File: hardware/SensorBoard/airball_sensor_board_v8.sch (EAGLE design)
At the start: 61 parts, among them IC1 CP2102, J2 USB Female Type C Connector, T1 BC846, T2 BC846, U1 BQ24075, U2 BQ27441-G1, U3 BMP388, U4 ESP-WROOM-32, U7 SP0503BAHT

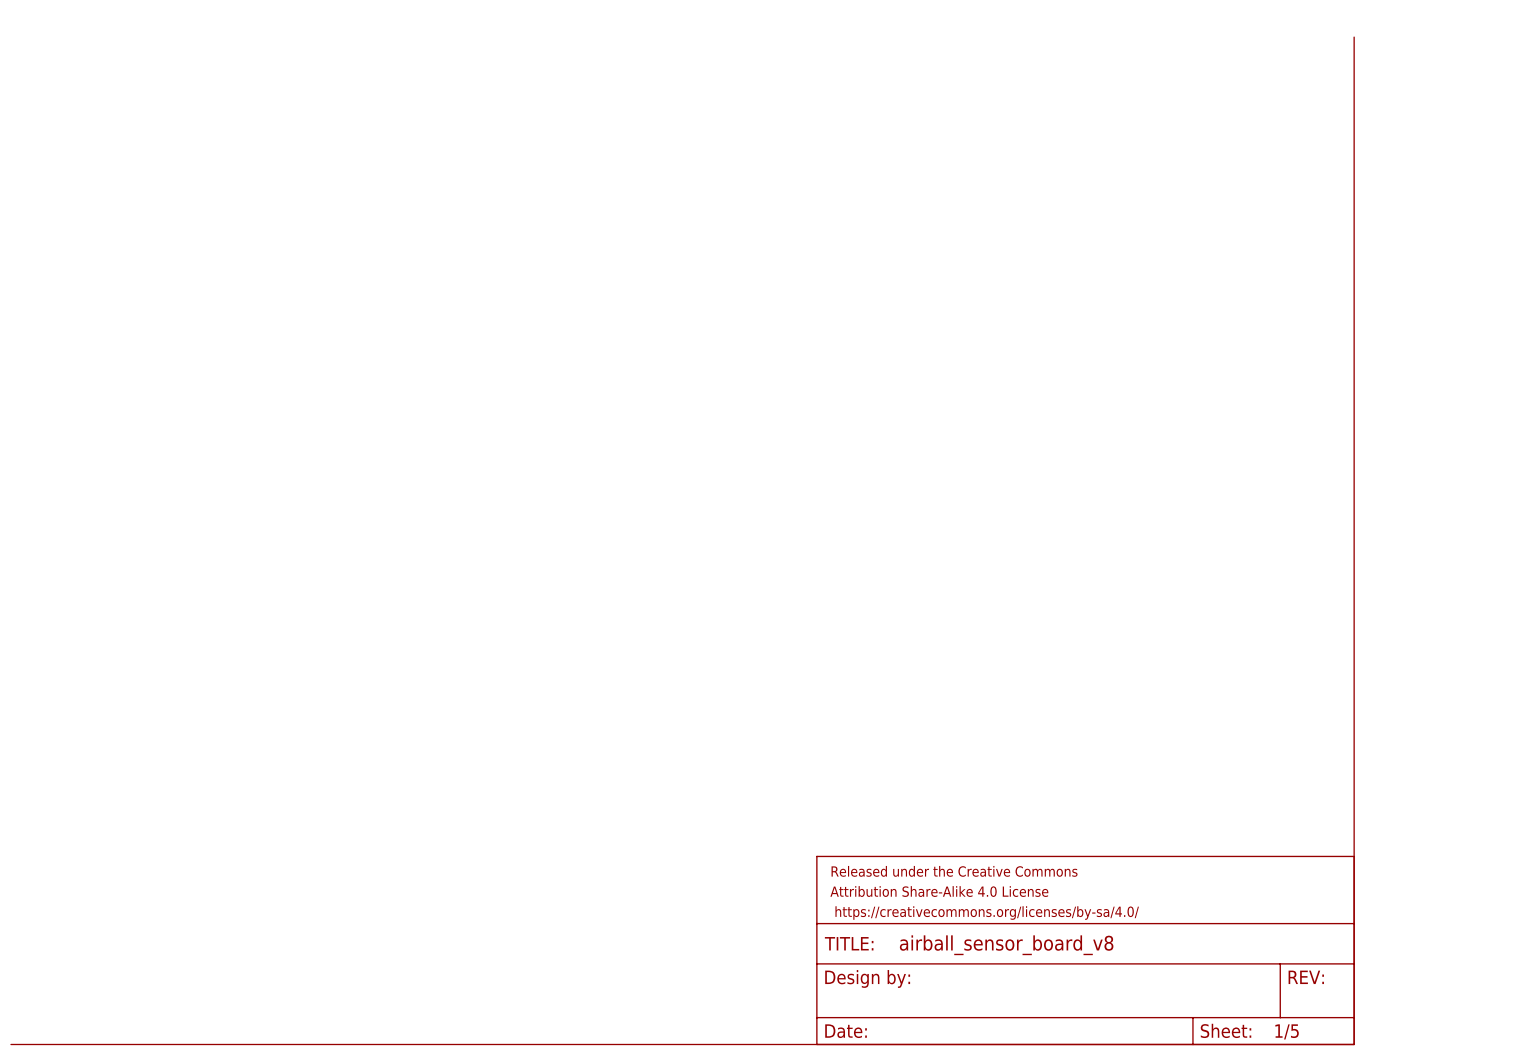
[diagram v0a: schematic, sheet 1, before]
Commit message: Formatting
Added titles and formatting to schematic and board.
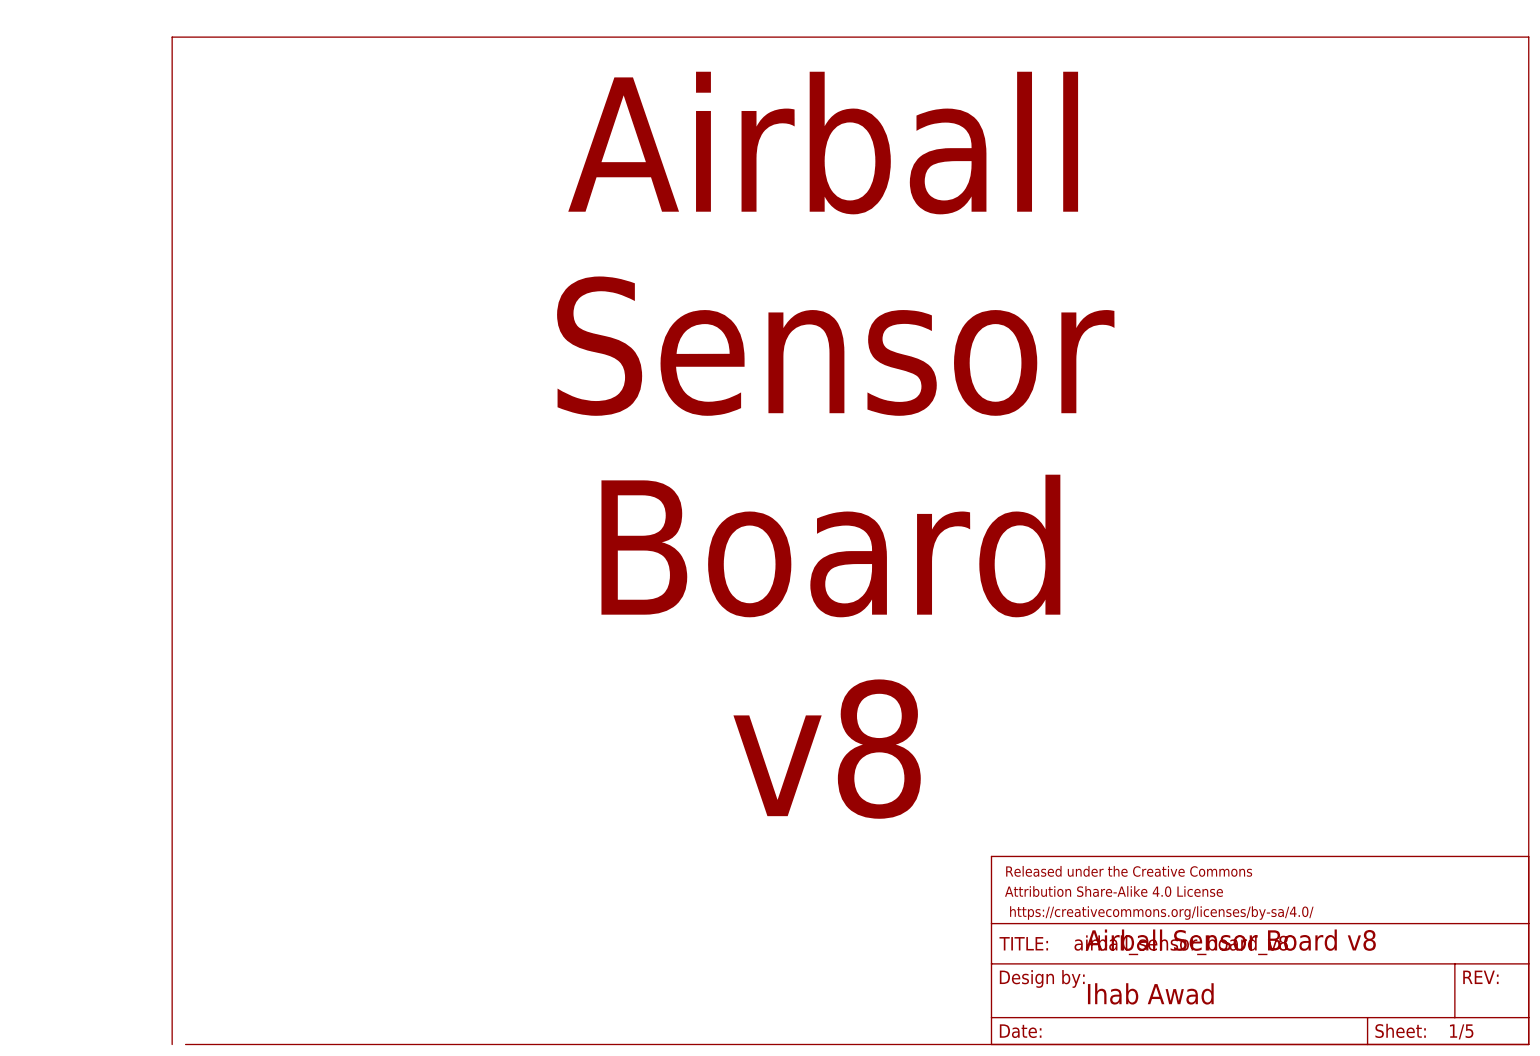
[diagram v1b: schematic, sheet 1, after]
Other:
- note added: "Airball Sensor Board v8"
- note added: "Ihab Awad"
- note added: "Power supply design is a copy of the Sparkfun "Battery Babysitter", designed by Jim Lindblom. See: https://www.sparkfun.com/products/13777"
- note removed: "Power supply design is a copy of the Sparkfun "Battery Babysitter", designed by Jim Lindblom."
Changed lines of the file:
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@@
 <sheet>
 <plain>
-<wire x1="223.52" y1="190.5" x2="223.52" y2="0" width="0.1524" layer="94"/>
-<wire x1="223.52" y1="0" x2="-30.48" y2="0" width="0.1524" layer="94"/>
+<wire x1="256.54" y1="190.5" x2="256.54" y2="0" width="0.1524" layer="94"/>
+<wire x1="256.54" y1="0" x2="2.54" y2="0" width="0.1524" layer="94"/>
+<wire x1="0" y1="0" x2="0" y2="190.5" width="0.1524" layer="94"/>
+<wire x1="0" y1="190.5" x2="256.54" y2="190.5" width="0.1524" layer="94"/>
+<text x="172.72" y="17.78" size="3.81" layer="94">Airball Sensor Board v8</text>
+<text x="172.72" y="7.62" size="3.81" layer="94">Ihab Awad</text>
+<text x="124.46" y="43.18" size="25.4" layer="94" align="bottom-center">Airball
+Sensor
+Board
+v8</text>
 </plain>
 <instances>
-<instance part="FRAME1" gate="V" x="121.92" y="0" smashed="yes"/>
+<instance part="FRAME1" gate="V" x="154.94" y="0" smashed="yes"/>
 </instances>
 <busses>
@@
 <text x="88.9" y="111.76" size="1.524" layer="97" font="vector" align="top-left">I2C ADDR: 0x55</text>
 <text x="119.38" y="124.46" size="6.35" layer="94" align="top-center">Power</text>
-<text x="165.1" y="114.3" size="2.54" layer="94">Power supply design is a copy of
+<text x="144.78" y="111.76" size="2.54" layer="94">Power supply design is a copy of
 the Sparkfun "Battery Babysitter",
-designed by Jim Lindblom.</text>
+designed by Jim Lindblom. See:
+https://www.sparkfun.com/products/13777</text>
 <text x="27.94" y="114.3" size="1.778" layer="94">R17 is 1206
 Current Sense

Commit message: Finishing touches to the board, sent to manufacturing.
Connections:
- net V_SUPPLY_UNREG: now also J4.2
- net V_USB: no longer J4.2
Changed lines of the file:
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@@
 <?xml version="1.0" encoding="utf-8"?>
 <!DOCTYPE eagle SYSTEM "eagle.dtd">
-<eagle version="9.6.0">
+<eagle version="9.6.2">
 <drawing>
 <settings>
@@
 <classes>
 <class number="0" name="default" width="0" drill="0">
+<clearance class="0" value="0.205"/>
 </class>
 </classes>
@@
 <wire x1="44.704" y1="95.25" x2="43.434" y2="92.71" width="0.1524" layer="94"/>
 <wire x1="0" y1="129.54" x2="0" y2="0" width="0.1524" layer="94"/>
-<wire x1="0" y1="0" x2="248.92" y2="0" width="0.1524" layer="94"/>
-<wire x1="248.92" y1="0" x2="248.92" y2="129.54" width="0.1524" layer="94"/>
-<wire x1="248.92" y1="129.54" x2="0" y2="129.54" width="0.1524" layer="94"/>
+<wire x1="0" y1="0" x2="256.54" y2="0" width="0.1524" layer="94"/>
+<wire x1="256.54" y1="0" x2="256.54" y2="129.54" width="0.1524" layer="94"/>
+<wire x1="256.54" y1="129.54" x2="0" y2="129.54" width="0.1524" layer="94"/>
 <wire x1="118.11" y1="52.324" x2="125.73" y2="52.324" width="0.1524" layer="94"/>
 <wire x1="123.19" y1="53.594" x2="125.73" y2="52.324" width="0.1524" layer="94"/>
@@
 <segment>
 <pinref part="U1" gate="G$1" pin="SYSOFF"/>
-<label x="226.06" y="60.96" size="1.27" layer="95" font="vector" xref="yes"/>
+<label x="226.06" y="60.96" size="1.778" layer="95" font="vector" xref="yes"/>
 <wire x1="109.22" y1="38.1" x2="111.76" y2="38.1" width="0.1524" layer="91"/>
 <wire x1="111.76" y1="38.1" x2="111.76" y2="60.96" width="0.1524" layer="91"/>
@@
 <junction x="129.54" y="50.8"/>
 <wire x1="129.54" y1="40.64" x2="127" y2="40.64" width="0.1524" layer="91"/>
+<wire x1="167.64" y1="50.8" x2="167.64" y2="55.88" width="0.1524" layer="91"/>
+<wire x1="167.64" y1="55.88" x2="226.06" y2="55.88" width="0.1524" layer="91"/>
+<label x="226.06" y="55.88" size="1.778" layer="95" xref="yes"/>
 </segment>
 </net>
@@
 <pinref part="U$1" gate="G$1" pin="OUT"/>
 <label x="226.06" y="50.8" size="1.778" layer="95" xref="yes"/>
-<pinref part="C4" gate="G$1" pin="1"/>
+<wire x1="198.12" y1="50.8" x2="200.66" y2="50.8" width="0.1524" layer="91"/>
 <wire x1="200.66" y1="50.8" x2="213.36" y2="50.8" width="0.1524" layer="91"/>
 <wire x1="213.36" y1="50.8" x2="226.06" y2="50.8" width="0.1524" layer="91"/>
-<wire x1="198.12" y1="50.8" x2="200.66" y2="50.8" width="0.1524" layer="91"/>
-<wire x1="200.66" y1="50.8" x2="200.66" y2="25.4" width="0.1524" layer="91"/>
 <pinref part="D3" gate="G$1" pin="A"/>
 <wire x1="213.36" y1="48.26" x2="213.36" y2="50.8" width="0.1524" layer="91"/>
@@
 <wire x1="213.36" y1="50.8" x2="213.36" y2="91.44" width="0.1524" layer="91"/>
 <wire x1="213.36" y1="91.44" x2="137.16" y2="91.44" width="0.1524" layer="91"/>
+<pinref part="C4" gate="G$1" pin="1"/>
+<wire x1="200.66" y1="25.4" x2="200.66" y2="50.8" width="0.1524" layer="91"/>
+<junction x="200.66" y="50.8"/>
 </segment>
 </net>
@@
 <attribute name="VALUE" x="95.5013" y="17.759490625" size="1.0162" layer="96" rot="R90"/>
 </instance>
-<instance part="GND26" gate="1" x="78.74" y="12.7" smashed="yes">
-<attribute name="VALUE" x="76.2" y="10.16" size="1.778" layer="96"/>
+<instance part="GND26" gate="1" x="78.74" y="10.16" smashed="yes">
+<attribute name="VALUE" x="76.2" y="7.62" size="1.778" layer="96"/>
 </instance>
 <instance part="GND5" gate="1" x="137.16" y="58.42" smashed="yes">
@@
 <pinref part="GND26" gate="1" pin="GND"/>
 <wire x1="83.82" y1="17.78" x2="78.74" y2="17.78" width="0.1524" layer="91"/>
-<wire x1="78.74" y1="17.78" x2="78.74" y2="15.24" width="0.1524" layer="91"/>
+<wire x1="78.74" y1="17.78" x2="78.74" y2="12.7" width="0.1524" layer="91"/>
 </segment>
 <segment>
@@
 <segment>
 <pinref part="J2" gate="J1" pin="VBUS"/>
-<wire x1="40.64" y1="38.1" x2="45.72" y2="38.1" width="0.1524" layer="91"/>
 <pinref part="U7" gate="G$1" pin="C"/>
-<wire x1="45.72" y1="38.1" x2="91.44" y2="38.1" width="0.1524" layer="91"/>
+<wire x1="40.64" y1="38.1" x2="91.44" y2="38.1" width="0.1524" layer="91"/>
 <wire x1="91.44" y1="25.4" x2="91.44" y2="38.1" width="0.1524" layer="91"/>
-<pinref part="J4" gate="J1" pin="2"/>
-<wire x1="33.02" y1="63.5" x2="45.72" y2="63.5" width="0.1524" layer="91"/>
-<wire x1="45.72" y1="63.5" x2="45.72" y2="38.1" width="0.1524" layer="91"/>
-<junction x="45.72" y="38.1"/>
 </segment>
 </net>
@@
 </segment>
 </net>
-<net name="N$3" class="0">
-<segment>
-<junction x="10.16" y="45.72"/>
-</segment>
-</net>
 <net name="N$13" class="0">
 <segment>
@@
 </segment>
 </net>
+<net name="V_SUPPLY_UNREG" class="0">
+<segment>
+<pinref part="J4" gate="J1" pin="2"/>
+<wire x1="33.02" y1="63.5" x2="45.72" y2="63.5" width="0.1524" layer="91"/>
+<label x="45.72" y="60.96" size="1.778" layer="95" xref="yes"/>
+<wire x1="45.72" y1="63.5" x2="45.72" y2="60.96" width="0.1524" layer="91"/>
+</segment>
+</net>
